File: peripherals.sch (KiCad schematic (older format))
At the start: 40 parts, among them J1 693022010811

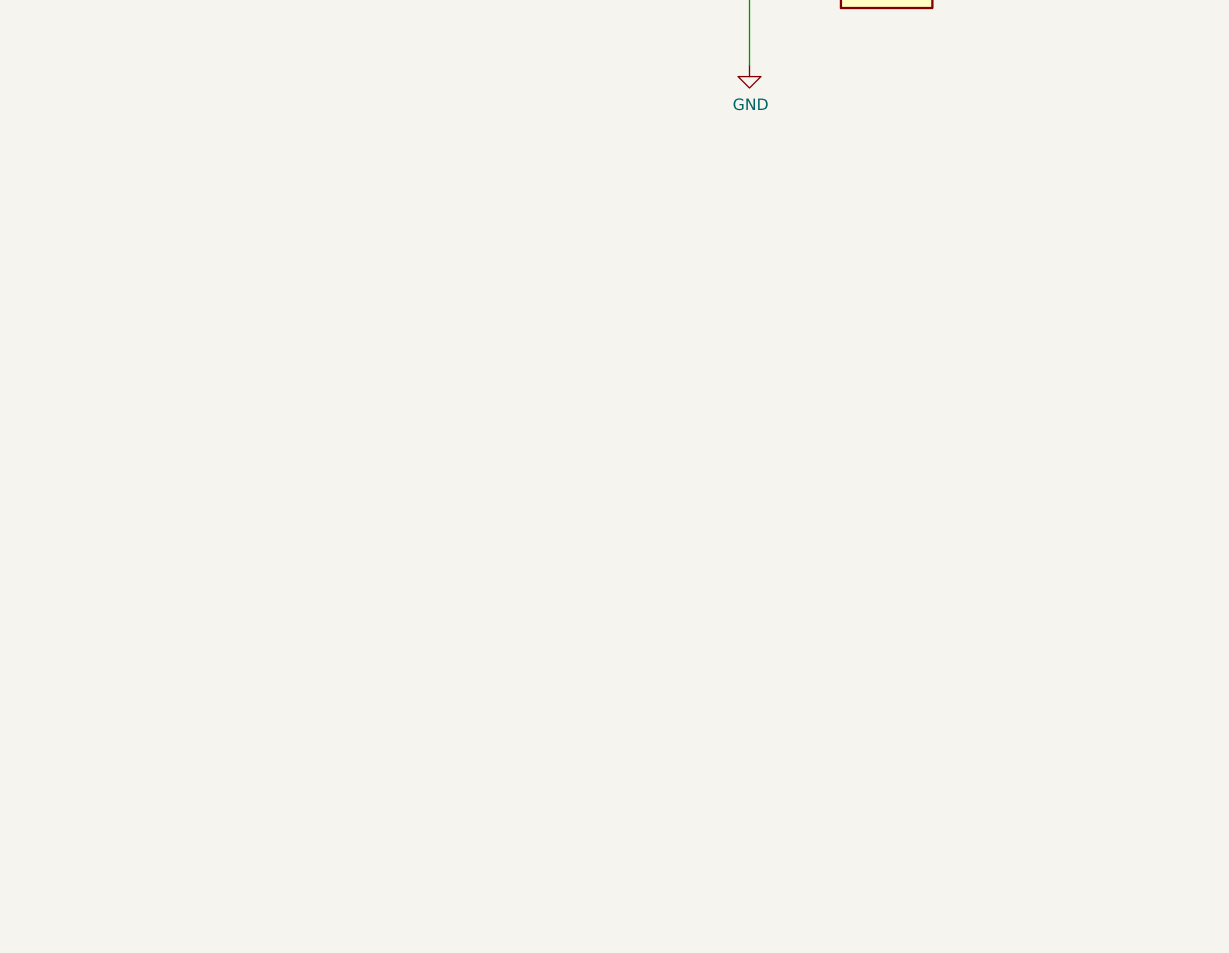
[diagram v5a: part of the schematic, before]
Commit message: Added TP Interface. Connector must yet be added
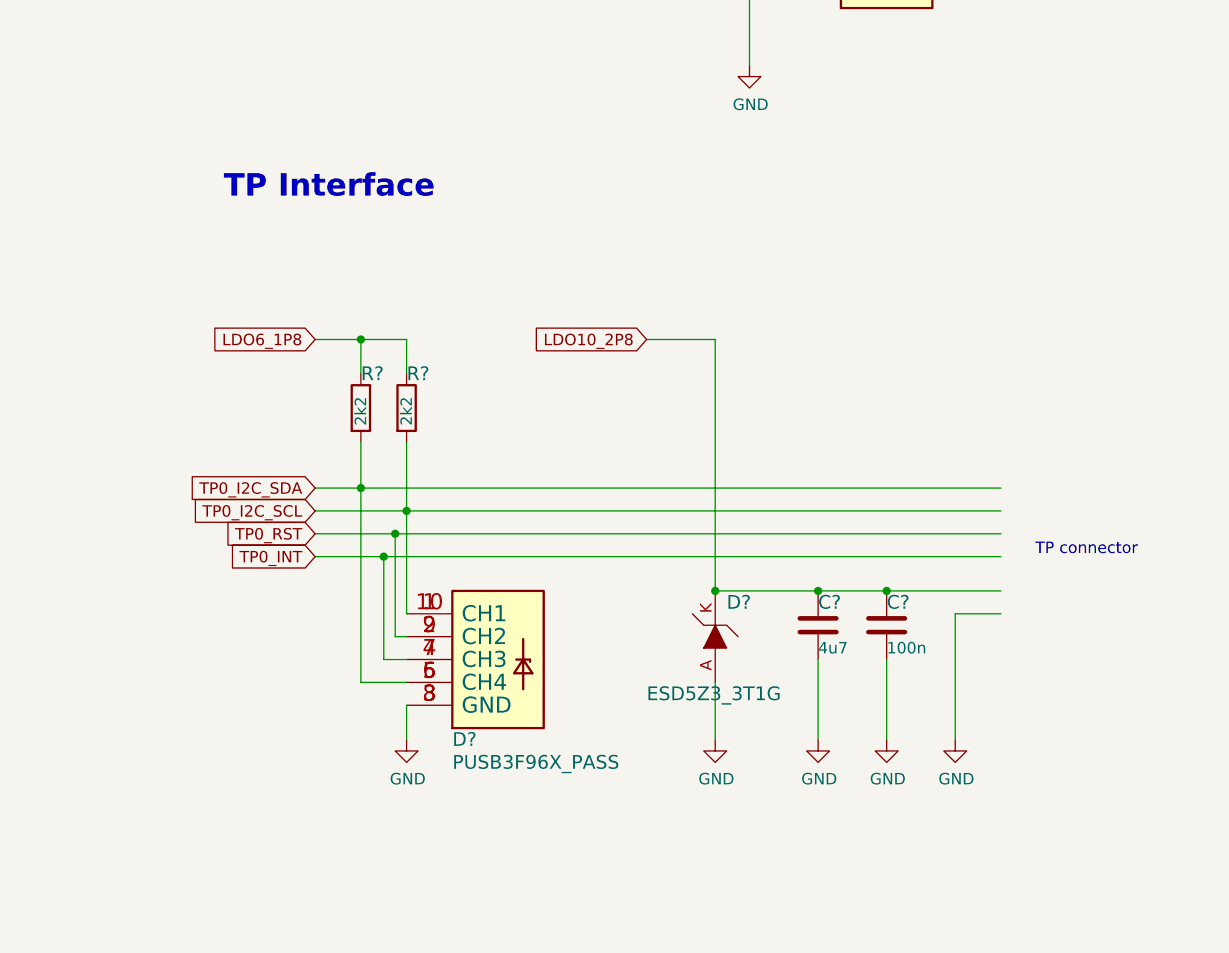
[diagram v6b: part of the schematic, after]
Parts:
- added C?: C_4u7_0402, antmicro-footprints:0402-cap, symbol antmicroCapacitors0402:C_4u7_0402
- added C?: C_100n_0402, antmicro-footprints:0402-cap, symbol antmicroCapacitors0402:C_100n_0402
- added D?: PUSB3F96X_PASS, antmicro-footprints:PUSB3F96X, symbol antmicroTVSDiodes:PUSB3F96X_PASS
- added D?: ESD5Z3_3T1G, antmicro-footprints:SOD-523, symbol antmicroTVSDiodes:ESD5Z3_3T1G
- added R? (x2): R_2k2_0402, antmicro-footprints:0402-res, symbol antmicroResistors0402:R_2k2_0402
- U?: footprint (none) -> antmicro-footprints:UFDFN-16_3.5x1.2mm
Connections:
- net labels added: LDO10_2P8, LDO6_1P8, TP0_I2C_SCL, TP0_I2C_SDA, TP0_INT, TP0_RST
- wire segments 118 -> 150
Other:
- note added: "TP Interface\n\n"
- note added: "TP connector\n"
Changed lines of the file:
@@
 F 0 "U?" H 2400 2800 50  0000 C CNN
 F 1 "EMIF06-MSD02N16" H 2700 2700 50  0000 C CNN
-F 2 "" H 2600 2750 50  0001 C CNN
+F 2 "antmicro-footprints:UFDFN-16_3.5x1.2mm" H 2600 2750 50  0001 C CNN
 F 3 "https://www.st.com/en/protections-and-emi-filters/emif06-msd02n16.html#overview" H 2600 2750 50  0001 C CNN
 F 4 "STMicroelectronics" H 2700 1300 50  0001 C CNN "Manufacturer"
@@
 	2150 1550 2250 1550
 NoConn ~ 2250 1650
+Text Notes 6900 4500 0    98   ~ 20
+TP Interface\n\n
+$Comp
+L antmicroTVSDiodes:PUSB3F96X_PASS D?
+U 1 1 61E35456
+P 7900 6350
+F 0 "D?" H 7900 6000 60  0000 L CNN
+F 1 "PUSB3F96X_PASS" H 7900 5900 60  0000 L CNN
+F 2 "antmicro-footprints:PUSB3F96X" H 8100 5800 60  0001 C CNN
+F 3 "https://pl.mouser.com/datasheet/2/916/PUSB3F96-1600324.pdf" H 7900 6350 60  0001 C CNN
+F 4 "Nexperia" H 8100 5700 50  0001 C CNN "Manufacturer"
+F 5 "PUSB3F96X" H 8100 5700 50  0001 C CNN "MPN"
+	1    7900 6350
+	1    0    0    -1
+$EndComp
+$Comp
+L antmicroTVSDiodes:ESD5Z3_3T1G D?
+U 1 1 61E3EF18
+P 9050 6250
+F 0 "D?" V 9200 6200 60  0000 R CNN
+F 1 "ESD5Z3_3T1G" V 8800 6550 60  0000 R CNN
+F 2 "antmicro-footprints:SOD-523" H 9250 6450 60  0001 L CNN
+F 3 "https://www.onsemi.com/pub/Collateral/ESD5Z2.5T1-D.PDF" H 9250 6550 60  0001 L CNN
+F 4 "ON Semiconductor" H 9250 7350 60  0001 L CNN "Manufacturer"
+F 5 "ESD5Z3.3T1G" H 9250 6750 60  0001 L CNN "MPN"
+	1    9050 6250
+	0    -1   -1   0
+$EndComp
+Text GLabel 7300 5700 0    50   Input ~ 0
+TP0_I2C_SCL
+Text GLabel 7300 5600 0    50   Input ~ 0
+TP0_I2C_SDA
+Text GLabel 7300 5800 0    50   Input ~ 0
+TP0_RST
+Text GLabel 7300 5900 0    50   Input ~ 0
+TP0_INT
+Text GLabel 7300 4950 0    50   Input ~ 0
+LDO6_1P8
+$Comp
+L antmicroResistors0402:R_2k2_0402 R?
+U 1 1 61ED0D15
+P 7500 5250
+F 0 "R?" V 7350 5250 60  0000 L CNN
+F 1 "R_2k2_0402" H 7500 5100 60  0001 C CNN
+F 2 "antmicro-footprints:0402-res" H 7700 5450 60  0001 L CNN
+F 3 "" H 7500 5250 50  0001 C CNN
+F 4 "YAGEO" H 7700 5650 60  0001 L CNN "Manufacturer"
+F 5 "RC0402FR-072K2L" H 7700 5550 60  0001 L CNN "MPN"
+F 6 "2k2" H 7450 5250 50  0000 L CNN "Val"
+	1    7500 5250
+	0    1    1    0
+$EndComp
+$Comp
+L antmicroResistors0402:R_2k2_0402 R?
+U 1 1 61ED1A24
+P 7700 5250
+F 0 "R?" V 7550 5250 60  0000 L CNN
+F 1 "R_2k2_0402" H 7700 5100 60  0001 C CNN
+F 2 "antmicro-footprints:0402-res" H 7900 5450 60  0001 L CNN
+F 3 "" H 7700 5250 50  0001 C CNN
+F 4 "YAGEO" H 7900 5650 60  0001 L CNN "Manufacturer"
+F 5 "RC0402FR-072K2L" H 7900 5550 60  0001 L CNN "MPN"
+F 6 "2k2" H 7650 5250 50  0000 L CNN "Val"
+	1    7700 5250
+	0    1    1    0
+$EndComp
+Wire Wire Line
+	7700 5100 7700 4950
+Wire Wire Line
+	7700 4950 7500 4950
+Wire Wire Line
+	7500 5100 7500 4950
+Connection ~ 7500 4950
+Wire Wire Line
+	7500 4950 7300 4950
+Wire Wire Line
+	7300 5600 7500 5600
+Wire Wire Line
+	7500 5600 7500 5400
+Wire Wire Line
+	7300 5700 7700 5700
+Wire Wire Line
+	7700 5700 7700 5400
+Connection ~ 7500 5600
+Wire Wire Line
+	7700 6150 7700 5700
+Connection ~ 7700 5700
+Wire Wire Line
+	7500 6450 7700 6450
+Wire Wire Line
+	7500 5600 7500 6450
+Wire Wire Line
+	7700 6350 7600 6350
+Wire Wire Line
+	7600 6350 7600 5900
+Wire Wire Line
+	7600 5900 7300 5900
+Wire Wire Line
+	7300 5800 7650 5800
+Wire Wire Line
+	7650 5800 7650 6250
+Wire Wire Line
+	7650 6250 7700 6250
+$Comp
+L power:GND #PWR?
+U 1 1 61F04AE8
+P 7700 6700
+F 0 "#PWR?" H 7700 6450 50  0001 C CNN
+F 1 "GND" H 7705 6527 50  0000 C CNN
+F 2 "" H 7700 6700 50  0001 C CNN
+F 3 "" H 7700 6700 50  0001 C CNN
+	1    7700 6700
+	1    0    0    -1
+$EndComp
+Wire Wire Line
+	7700 6550 7700 6700
+Text GLabel 8750 4950 0    50   Input ~ 0
+LDO10_2P8
+$Comp
+L power:GND #PWR?
+U 1 1 61F2FE2E
+P 9050 6700
+F 0 "#PWR?" H 9050 6450 50  0001 C CNN
+F 1 "GND" H 9055 6527 50  0000 C CNN
+F 2 "" H 9050 6700 50  0001 C CNN
+F 3 "" H 9050 6700 50  0001 C CNN
+	1    9050 6700
+	1    0    0    -1
+$EndComp
+Wire Wire Line
+	9050 6700 9050 6450
+Wire Wire Line
+	9050 6050 9050 4950
+Wire Wire Line
+	9050 4950 8750 4950
+$Comp
+L antmicroCapacitors0402:C_4u7_0402 C?
+U 1 1 61F3D459
+P 9500 6200
+F 0 "C?" H 9500 6300 60  0000 L CNN
+F 1 "C_4u7_0402" H 9500 6050 60  0001 C CNN
+F 2 "antmicro-footprints:0402-cap" H 9700 6400 60  0001 L CNN
+F 3 "" H 9500 6200 50  0001 C CNN
+F 4 "MURATA" H 9700 6600 60  0001 L CNN "Manufacturer"
+F 5 "GRM155R61A475MEAAD" H 9700 6500 60  0001 L CNN "MPN"
+F 6 "4u7" H 9500 6100 50  0000 L CNN "Val"
+	1    9500 6200
+	1    0    0    -1
+$EndComp
+$Comp
+L antmicroCapacitors0402:C_100n_0402 C?
+U 1 1 61F3E80F
+P 9800 6200
+F 0 "C?" H 9800 6300 60  0000 L CNN
+F 1 "C_100n_0402" H 9800 6050 60  0001 C CNN
+F 2 "antmicro-footprints:0402-cap" H 10000 6400 60  0001 L CNN
+F 3 "" H 9800 6200 50  0001 C CNN
+F 4 "Murata" H 10000 6600 60  0001 L CNN "Manufacturer"
+F 5 "GRM155R61H104KE14D" H 10000 6500 60  0001 L CNN "MPN"
+F 6 "100n" H 9800 6100 50  0000 L CNN "Val"
+	1    9800 6200
+	1    0    0    -1
+$EndComp
+$Comp
+L power:GND #PWR?
+U 1 1 61F3F968
+P 9500 6700
+F 0 "#PWR?" H 9500 6450 50  0001 C CNN
+F 1 "GND" H 9505 6527 50  0000 C CNN
+F 2 "" H 9500 6700 50  0001 C CNN
+F 3 "" H 9500 6700 50  0001 C CNN
+	1    9500 6700
+	1    0    0    -1
+$EndComp
+$Comp
+L power:GND #PWR?
+U 1 1 61F3FF72
+P 9800 6700
+F 0 "#PWR?" H 9800 6450 50  0001 C CNN
+F 1 "GND" H 9805 6527 50  0000 C CNN
+F 2 "" H 9800 6700 50  0001 C CNN
+F 3 "" H 9800 6700 50  0001 C CNN
+	1    9800 6700
+	1    0    0    -1
+$EndComp
+Wire Wire Line
+	9800 6700 9800 6350
+Wire Wire Line
+	9500 6350 9500 6700
+Wire Wire Line
+	9800 6050 9500 6050
+Wire Wire Line
+	9050 6050 9500 6050
+Connection ~ 9050 6050
+Connection ~ 9500 6050
+Wire Wire Line
+	7500 5600 10300 5600
+Wire Wire Line
+	7700 5700 10300 5700
+Wire Wire Line
+	7650 5800 10300 5800
+Connection ~ 7650 5800
+Wire Wire Line
+	7600 5900 10300 5900
+Connection ~ 7600 5900
+Wire Wire Line
+	9800 6050 10300 6050
+Connection ~ 9800 6050
+$Comp
+L power:GND #PWR?
+U 1 1 61F8A3E4
+P 10100 6700
+F 0 "#PWR?" H 10100 6450 50  0001 C CNN
+F 1 "GND" H 10105 6527 50  0000 C CNN
+F 2 "" H 10100 6700 50  0001 C CNN
+F 3 "" H 10100 6700 50  0001 C CNN
+	1    10100 6700
+	1    0    0    -1
+$EndComp
+Wire Wire Line
+	10100 6700 10100 6150
+Wire Wire Line
+	10100 6150 10300 6150
 Wire Bus Line
 	700  1450 700  2150
+Text Notes 10450 5900 0    50   ~ 0
+TP connector\n
 $EndSCHEMATC

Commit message: Added annotations. Move to loclib
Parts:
- ANT1: renamed from ANT?; footprint antmicro-footprints:GPS-ANT050-mounting-pad -> sc606-baseboard-footprints:GPS-ANT050-mounting-pad; symbol antmicroRFAntennas:GPS-ANT050-external-antenna -> sc606-baseboard:GPS-ANT050-external-antenna
- ANT2: renamed from ANT?; footprint antmicro-footprints:PRO-OB-572_2 -> sc606-baseboard-footprints:PRO-OB-572_2; symbol antmicroRFAntennas:PRO-OB-572_DCPOL -> sc606-baseboard:PRO-OB-572_DCPOL
- C34, C46, C53, C56: renamed from C?; footprint antmicro-footprints:0402-cap -> sc606-baseboard-footprints:0402-cap; symbol antmicroCapacitors0402:C_100n_0402 -> sc606-baseboard:C_100n_0402
- C35, C42, C43: renamed from C?; footprint antmicro-footprints:0402-cap -> sc606-baseboard-footprints:0402-cap; symbol antmicroCapacitors0402:C_1u_0402 -> sc606-baseboard:C_1u_0402
- C36, C38, C40, C45, C49, C50: renamed from C?; footprint antmicro-footprints:0402-cap -> sc606-baseboard-footprints:0402-cap; symbol antmicroCapacitors0402:C_0p5_0402 -> sc606-baseboard:C_0p5_0402
- C37, C41: renamed from C?; footprint antmicro-footprints:0402-cap -> sc606-baseboard-footprints:0402-cap; symbol antmicroCapacitors0402:C_0p9_0402 -> sc606-baseboard:C_0p9_0402
- C39: renamed from C?; footprint antmicro-footprints:0402-cap -> sc606-baseboard-footprints:0402-cap; symbol antmicroCapacitors0402:C_6p9_0402 -> sc606-baseboard:C_6p9_0402
- C44: renamed from C?; footprint antmicro-footprints:0402-cap -> sc606-baseboard-footprints:0402-cap; symbol antmicroCapacitors0402:C_33p_0402 -> sc606-baseboard:C_33p_0402
- C47, C55: renamed from C?; footprint antmicro-footprints:0402-cap -> sc606-baseboard-footprints:0402-cap; symbol antmicroCapacitors0402:C_4u7_0402 -> sc606-baseboard:C_4u7_0402
- C48: renamed from C?; footprint antmicro-footprints:0402-cap -> sc606-baseboard-footprints:0402-cap; symbol antmicroCapacitors0402:C_100p_0402 -> sc606-baseboard:C_100p_0402
- C51, C52, C54: renamed from C?; footprint antmicro-footprints:0402-cap -> sc606-baseboard-footprints:0402-cap; symbol antmicroCapacitors0402:C_22p_0402 -> sc606-baseboard:C_22p_0402
- D2: footprint antmicro-footprints:PUSB3F96X -> sc606-baseboard-footprints:PUSB3F96X; symbol antmicroTVSDiodes:PUSB3F96X_PASS -> sc606-baseboard:PUSB3F96X_PASS
- D5: renamed from D?; footprint antmicro-footprints:PUSB3F96X -> sc606-baseboard-footprints:PUSB3F96X; symbol antmicroTVSDiodes:PUSB3F96X_PASS -> sc606-baseboard:PUSB3F96X_PASS
- D6: renamed from D?; footprint antmicro-footprints:SOD-523 -> sc606-baseboard-footprints:SOD-523; symbol antmicroTVSDiodes:ESD5Z3_3T1G -> sc606-baseboard:ESD5Z3_3T1G
- J1: footprint antmicro-footprints:693022010811 -> sc606-baseboard-footprints:693022010811; symbol antmicroSimCardConnectors:693022010811 -> sc606-baseboard:693022010811
- J5, J6: renamed from J?; footprint antmicro-footprints:Coax_Conn_U.FL -> sc606-baseboard-footprints:Coax_Conn_U.FL; symbol antmicroCoaxialConnectorsRF:U_FL-R-SMT-1_10_ -> sc606-baseboard:U_FL-R-SMT-1_10_
- J7: renamed from J?; footprint antmicro-footprints:MicroSD_DM3AT-SF-PEJM5 -> sc606-baseboard-footprints:MicroSD_DM3AT-SF-PEJM5; symbol antmicroMemoryConnectorsPCCardSockets:DM3AT-SF-PEJM5 -> sc606-baseboard:DM3AT-SF-PEJM5
- L4: renamed from L?; footprint antmicro-footprints:0402-res -> sc606-baseboard-footprints:0402-res; symbol antmicroFixedInductors:LQW15AN2N4B00D -> sc606-baseboard:LQW15AN2N4B00D
- L5: renamed from L?; footprint antmicro-footprints:0402-res -> sc606-baseboard-footprints:0402-res; symbol antmicroFixedInductors:MLJ1005HXG56NETD0B -> sc606-baseboard:MLJ1005HXG56NETD0B
- R31, R33: renamed from R?; footprint antmicro-footprints:0402-res -> sc606-baseboard-footprints:0402-res; symbol antmicroResistors0402:R_0R_0402 -> sc606-baseboard:R_0R_0402
- R32, R40: renamed from R?; footprint antmicro-footprints:0402-res -> sc606-baseboard-footprints:0402-res; symbol antmicroResistors0402:R_10k_0402 -> sc606-baseboard:R_10k_0402
- R34: renamed from R?; footprint antmicro-footprints:0603-res -> sc606-baseboard-footprints:0603-res; symbol antmicroResistors0603:R_10R_0603 -> sc606-baseboard:R_10R_0603
- R35, R39: renamed from R?; footprint antmicro-footprints:0402-res -> sc606-baseboard-footprints:0402-res; symbol antmicroResistors0402:R_2k2_0402 -> sc606-baseboard:R_2k2_0402
- R36, R37, R38: renamed from R?; footprint antmicro-footprints:0402-res -> sc606-baseboard-footprints:0402-res; symbol antmicroResistors0402:R_22R_0402 -> sc606-baseboard:R_22R_0402
- U6: renamed from U?; footprint antmicro-footprints:SOT-23-5 -> sc606-baseboard-footprints:SOT-23-5; symbol antmicroPMICVoltageRegulatorsLinear:NCP163ASN330T1G -> sc606-baseboard:NCP163ASN330T1G
- U7: renamed from U?; footprint antmicro-footprints:UFDFN-16_3.5x1.2mm -> sc606-baseboard-footprints:UFDFN-16_3.5x1.2mm; symbol antmicroPowerProtection:EMIF06-MSD02N16 -> sc606-baseboard:EMIF06-MSD02N16

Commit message: Block diagram update
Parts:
- ANT1: footprint sc606-baseboard-footprints:GPS-ANT050-mounting-pad -> antmicro-footprints:GPS-ANT050-mounting-pad; symbol sc606-baseboard:GPS-ANT050-external-antenna -> antmicroRFAntennas:GPS-ANT050-external-antenna
- ANT2: footprint sc606-baseboard-footprints:PRO-OB-572_2 -> antmicro-footprints:PRO-OB-572_2; symbol sc606-baseboard:PRO-OB-572_DCPOL -> antmicroRFAntennas:PRO-OB-572_DCPOL
- C34, C46, C53, C56: footprint sc606-baseboard-footprints:0402-cap -> antmicro-footprints:0402-cap; symbol sc606-baseboard:C_100n_0402 -> antmicroCapacitors0402:C_100n_0402
- C35, C42, C43: footprint sc606-baseboard-footprints:0402-cap -> antmicro-footprints:0402-cap; symbol sc606-baseboard:C_1u_0402 -> antmicroCapacitors0402:C_1u_0402
- C36, C38, C40, C45, C49, C50: footprint sc606-baseboard-footprints:0402-cap -> antmicro-footprints:0402-cap; symbol sc606-baseboard:C_0p5_0402 -> antmicroCapacitors0402:C_0p5_0402
- C37, C41: footprint sc606-baseboard-footprints:0402-cap -> antmicro-footprints:0402-cap; symbol sc606-baseboard:C_0p9_0402 -> antmicroCapacitors0402:C_0p9_0402
- C39: footprint sc606-baseboard-footprints:0402-cap -> antmicro-footprints:0402-cap; symbol sc606-baseboard:C_6p9_0402 -> antmicroCapacitors0402:C_6p9_0402
- C44: footprint sc606-baseboard-footprints:0402-cap -> antmicro-footprints:0402-cap; symbol sc606-baseboard:C_33p_0402 -> antmicroCapacitors0402:C_33p_0402
- C47, C55: footprint sc606-baseboard-footprints:0402-cap -> antmicro-footprints:0402-cap; symbol sc606-baseboard:C_4u7_0402 -> antmicroCapacitors0402:C_4u7_0402
- C48: footprint sc606-baseboard-footprints:0402-cap -> antmicro-footprints:0402-cap; symbol sc606-baseboard:C_100p_0402 -> antmicroCapacitors0402:C_100p_0402
- C51, C52, C54: footprint sc606-baseboard-footprints:0402-cap -> antmicro-footprints:0402-cap; symbol sc606-baseboard:C_22p_0402 -> antmicroCapacitors0402:C_22p_0402
- D2, D5: footprint sc606-baseboard-footprints:PUSB3F96X -> antmicro-footprints:PUSB3F96X; symbol sc606-baseboard:PUSB3F96X_PASS -> antmicroTVSDiodes:PUSB3F96X_PASS
- D6: footprint sc606-baseboard-footprints:SOD-523 -> antmicro-footprints:SOD-523; symbol sc606-baseboard:ESD5Z3_3T1G -> antmicroTVSDiodes:ESD5Z3_3T1G
- J1: footprint sc606-baseboard-footprints:693022010811 -> antmicro-footprints:693022010811; symbol sc606-baseboard:693022010811 -> antmicroSimCardConnectors:693022010811
- J5, J6: footprint sc606-baseboard-footprints:Coax_Conn_U.FL -> antmicro-footprints:Coax_Conn_U.FL; symbol sc606-baseboard:U_FL-R-SMT-1_10_ -> antmicroCoaxialConnectorsRF:U_FL-R-SMT-1_10_
- J7: footprint sc606-baseboard-footprints:MicroSD_DM3AT-SF-PEJM5 -> antmicro-footprints:MicroSD_DM3AT-SF-PEJM5; symbol sc606-baseboard:DM3AT-SF-PEJM5 -> antmicroMemoryConnectorsPCCardSockets:DM3AT-SF-PEJM5
- L4: footprint sc606-baseboard-footprints:0402-res -> antmicro-footprints:0402-res; symbol sc606-baseboard:LQW15AN2N4B00D -> antmicroFixedInductors:LQW15AN2N4B00D
- L5: footprint sc606-baseboard-footprints:0402-res -> antmicro-footprints:0402-res; symbol sc606-baseboard:MLJ1005HXG56NETD0B -> antmicroFixedInductors:MLJ1005HXG56NETD0B
- R31, R33: footprint sc606-baseboard-footprints:0402-res -> antmicro-footprints:0402-res; symbol sc606-baseboard:R_0R_0402 -> antmicroResistors0402:R_0R_0402
- R32, R40: footprint sc606-baseboard-footprints:0402-res -> antmicro-footprints:0402-res; symbol sc606-baseboard:R_10k_0402 -> antmicroResistors0402:R_10k_0402
- R34: footprint sc606-baseboard-footprints:0603-res -> antmicro-footprints:0603-res; symbol sc606-baseboard:R_10R_0603 -> antmicroResistors0603:R_10R_0603
- R35, R39: footprint sc606-baseboard-footprints:0402-res -> antmicro-footprints:0402-res; symbol sc606-baseboard:R_2k2_0402 -> antmicroResistors0402:R_2k2_0402
- R36, R37, R38: footprint sc606-baseboard-footprints:0402-res -> antmicro-footprints:0402-res; symbol sc606-baseboard:R_22R_0402 -> antmicroResistors0402:R_22R_0402
- U6: footprint sc606-baseboard-footprints:SOT-23-5 -> antmicro-footprints:SOT-23-5; symbol sc606-baseboard:NCP163ASN330T1G -> antmicroPMICVoltageRegulatorsLinear:NCP163ASN330T1G
- U7: footprint sc606-baseboard-footprints:UFDFN-16_3.5x1.2mm -> antmicro-footprints:UFDFN-16_3.5x1.2mm; symbol sc606-baseboard:EMIF06-MSD02N16 -> antmicroPowerProtection:EMIF06-MSD02N16
